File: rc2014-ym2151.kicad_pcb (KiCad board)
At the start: 2 copper layers, 100 x 50 mm, 36 parts, among them CON1 SJ1-3523N, J1 Conn_01x03, P1 RC2014 BUS, U1 74HCT688, U2 YM2151, U3 YM3012, U4 NJM4556, U5 NJM4556, X1 3.579545MHz

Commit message: add bits lurking around
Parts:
- C10, C11: footprint Capacitor_THT:CP_Radial_D7.5mm_P2.50mm -> Capacitor_THT:CP_Radial_D5.0mm_P2.50mm
- C7: footprint Capacitor_THT:C_Disc_D3.8mm_W2.6mm_P2.50mm -> Capacitor_THT:C_Radial_D4.0mm_H7.0mm_P1.50mm
- J1: footprint Connector_PinHeader_2.54mm:PinHeader_1x07_P2.54mm_Vertical -> Connector_PinHeader_2.54mm:PinHeader_1x06_P2.54mm_Vertical
- moved C7 1.56 mm to (104.0, 117.8)
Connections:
- J1 pad 3: /~IRQ -> GND
- J1 pad 4: GND -> VSS
- J1 pad 5: VSS -> VDD
- J1 pad 6: VDD -> VCC
- P1 pad 22: (no net) -> /~INT
- U2 pad 2: /~IRQ -> /~INT
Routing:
- net /~IRQ: track 41.7 -> 0.00 mm, vias 1 -> 0
- net /~INT: track 0.00 -> 11.0 mm, vias 0 -> 1
- net VSS: track 78.3 -> 75.8 mm
- net VCC: track 165.6 -> 163.1 mm
- net VDD: track 109.3 -> 106.8 mm
- net /RB: track 18.8 -> 20.5 mm
- net Net-(R1-Pad1): track 19.1 -> 20.1 mm
- net /~IORQ: track 50.8 -> 51.8 mm
- net /~CS: track 59.9 -> 60.5 mm
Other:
- board text added: "JLCJLCJLCJLC"
- board text removed: "~IRQ"

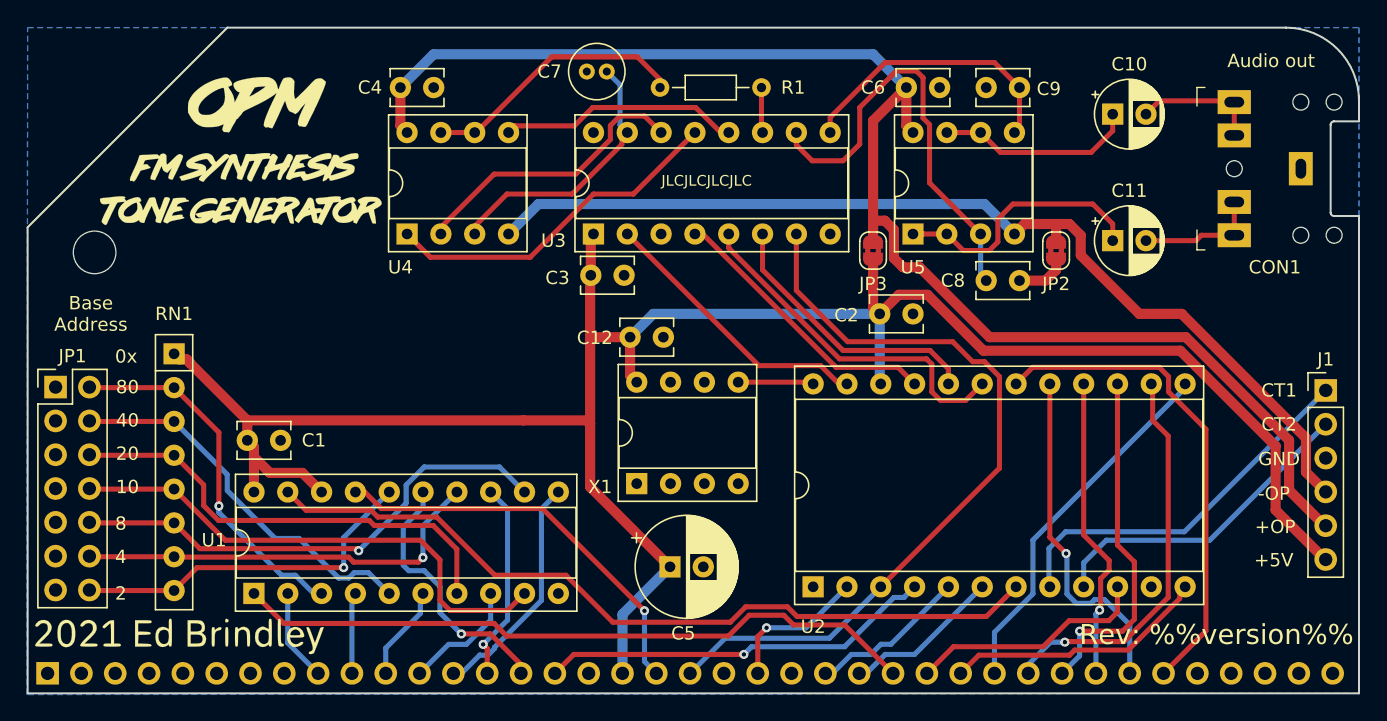
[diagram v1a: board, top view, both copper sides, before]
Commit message: Update to Kicad 6
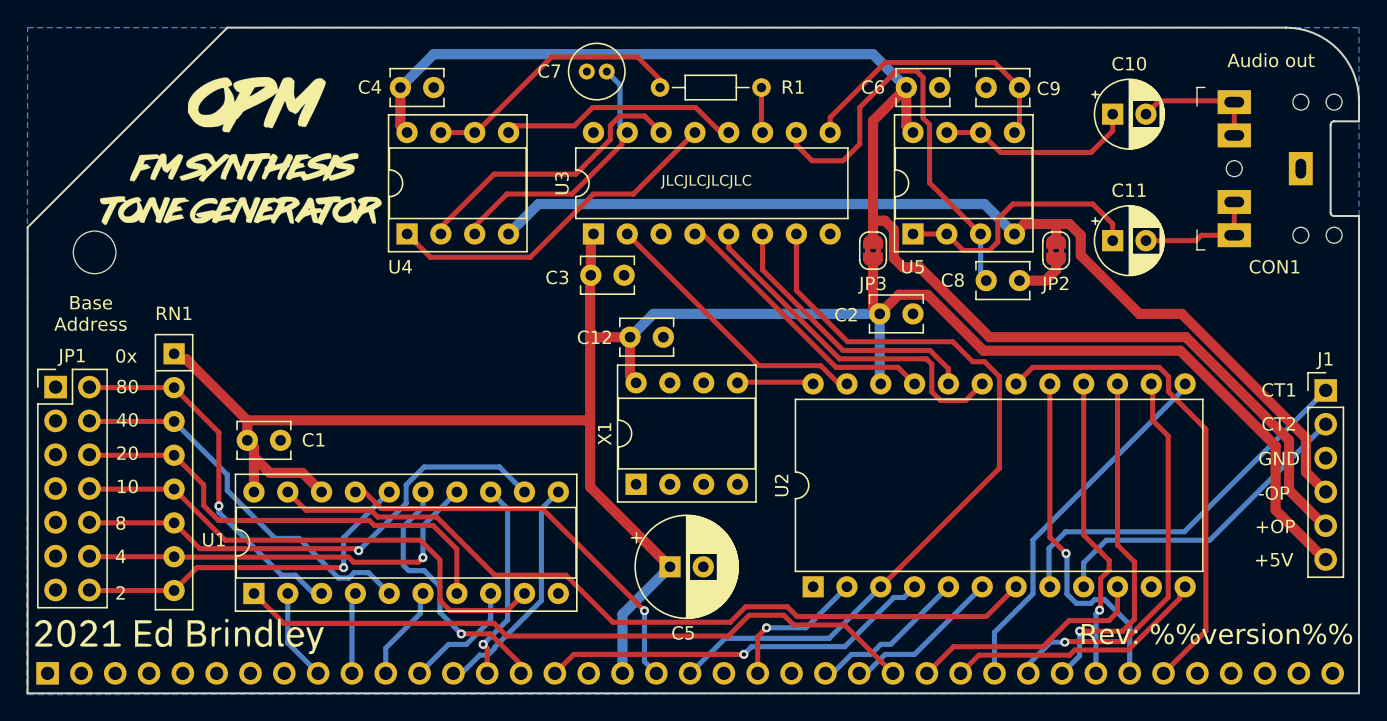
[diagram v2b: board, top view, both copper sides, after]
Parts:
- U2: footprint Package_DIP:DIP-24_W15.24mm_Socket -> Package_DIP:DIP-24_W15.24mm
- U3: footprint Package_DIP:DIP-16_W7.62mm_Socket -> Package_DIP:DIP-16_W7.62mm
- moved X1 0.07 mm to (106.2, 148.8)
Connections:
- net /~CS renamed /~{CS}
- net /~INT renamed /~{INT}
- net /~IORQ renamed /~{IORQ}
- net /~RD renamed /~{RD}
- net /~RESET renamed /~{RESET}
- net /~WR renamed /~{WR}
- P1 pad 1: (no net) -> unconnected-(P1-Pad1)
- P1 pad 2: (no net) -> unconnected-(P1-Pad2)
- P1 pad 21: (no net) -> unconnected-(P1-Pad21)
- P1 pad 23: (no net) -> unconnected-(P1-Pad23)
- P1 pad 3: (no net) -> unconnected-(P1-Pad3)
- P1 pad 35: (no net) -> unconnected-(P1-Pad35)
- P1 pad 36: (no net) -> unconnected-(P1-Pad36)
- P1 pad 37: (no net) -> unconnected-(P1-Pad37)
- P1 pad 38: (no net) -> unconnected-(P1-Pad38)
- P1 pad 39: (no net) -> unconnected-(P1-Pad39)
- P1 pad 4: (no net) -> unconnected-(P1-Pad4)
- P1 pad 5: (no net) -> unconnected-(P1-Pad5)
- P1 pad 6: (no net) -> unconnected-(P1-Pad6)
- P1 pad 7: (no net) -> unconnected-(P1-Pad7)
- P1 pad 8: (no net) -> unconnected-(P1-Pad8)
- X1 pad 1: (no net) -> unconnected-(X1-Pad1)
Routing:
- net /RB: track 20.5 -> 19.3 mm
- net VCC: track 163.1 -> 162.0 mm
- net /A1: track 19.9 -> 19.2 mm
- net Net-(JP1-Pad2): track 27.4 -> 26.7 mm
- net /A3: track 17.6 -> 17.0 mm
- net /R: track 19.8 -> 19.2 mm
- net /DAC_CLK: track 21.2 -> 20.6 mm
- net /TO_BUFF: track 18.1 -> 17.5 mm
- net /VOUT_CH1: track 32.8 -> 32.2 mm
- net /DAC_DATA: track 21.2 -> 20.6 mm
- net /D1: track 19.8 -> 19.3 mm
- net /VOUT_CH2: track 21.4 -> 20.8 mm
- net /~{WR}: track 11.9 -> 11.4 mm
- net /~{RD}: track 11.9 -> 11.4 mm
- net /BC: track 21.6 -> 21.1 mm
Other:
- net class Default removed
- net class IO removed
- net class analogue removed
- net class gnd removed
- net class vcc removed

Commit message: Tidy up schematic further
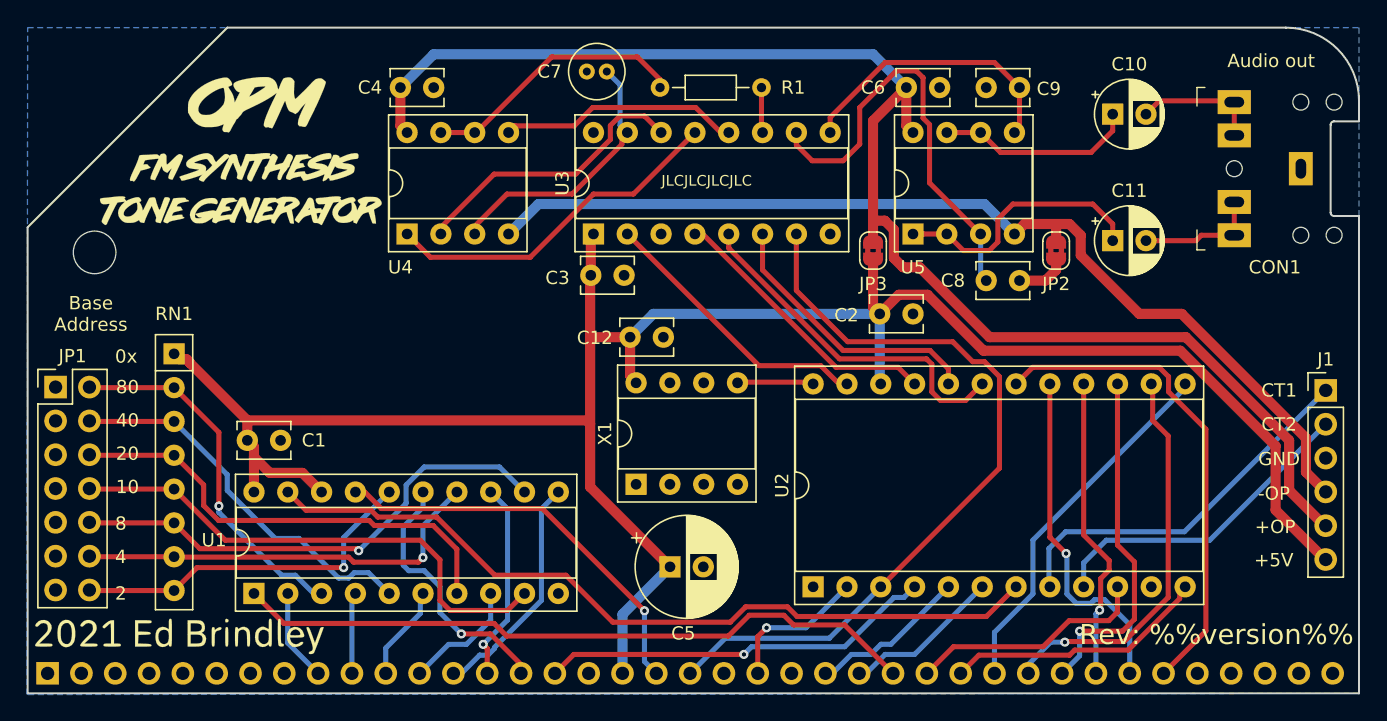
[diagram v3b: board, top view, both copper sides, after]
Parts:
- U2: footprint Package_DIP:DIP-24_W15.24mm -> Package_DIP:DIP-24_W15.24mm_Socket
- U3: footprint Package_DIP:DIP-16_W7.62mm -> Package_DIP:DIP-16_W7.62mm_Socket

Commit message: remove silk that clashes, another date fix
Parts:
- removed the G*** at (134.3, 148.8)

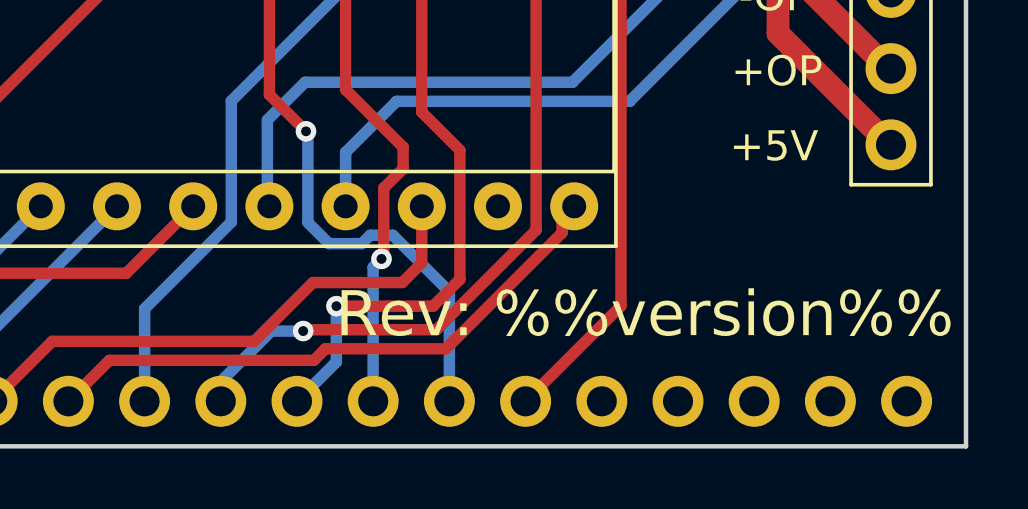
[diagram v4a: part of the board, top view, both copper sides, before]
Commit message: date replacement
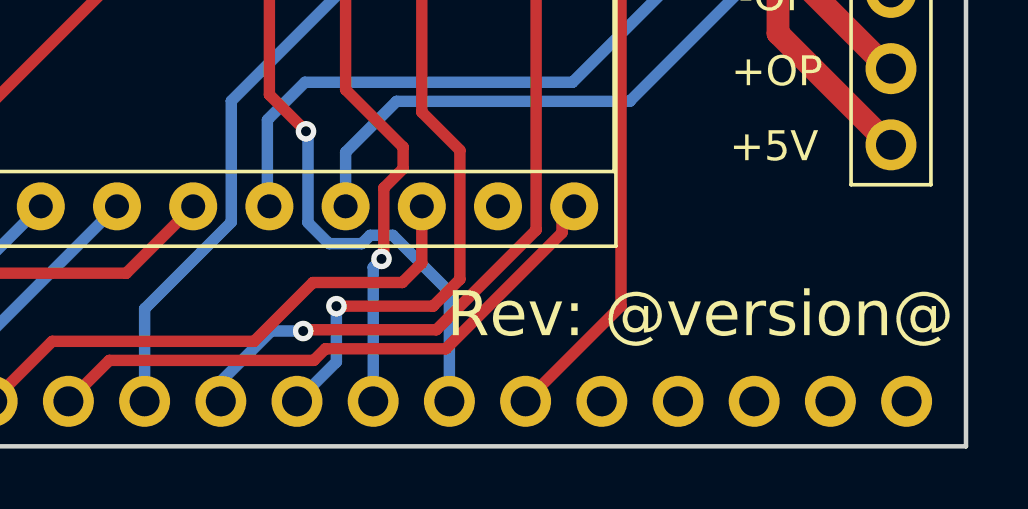
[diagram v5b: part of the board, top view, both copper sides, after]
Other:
- board text added: "Rev: @version@"
- board text removed: "Rev: %%version%%"
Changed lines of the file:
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@@
   (title_block
     (title "RC2014 YM2151 sound card")
-    (date "%%date%%")
-    (rev "%%version%%")
+    (date "@date@")
+    (rev "@version@")
   )
   (layers
@@
     (effects (font (size 1 1) (thickness 0.15)))
   )
-  (gr_text "Rev: %%version%%" (at 160.1 160.1) (layer "F.SilkS")
+  (gr_text "Rev: @version@" (at 160.1 160.1) (layer "F.SilkS")
     (effects (font (size 1.5 1.5) (thickness 0.3)) (justify right))
   )

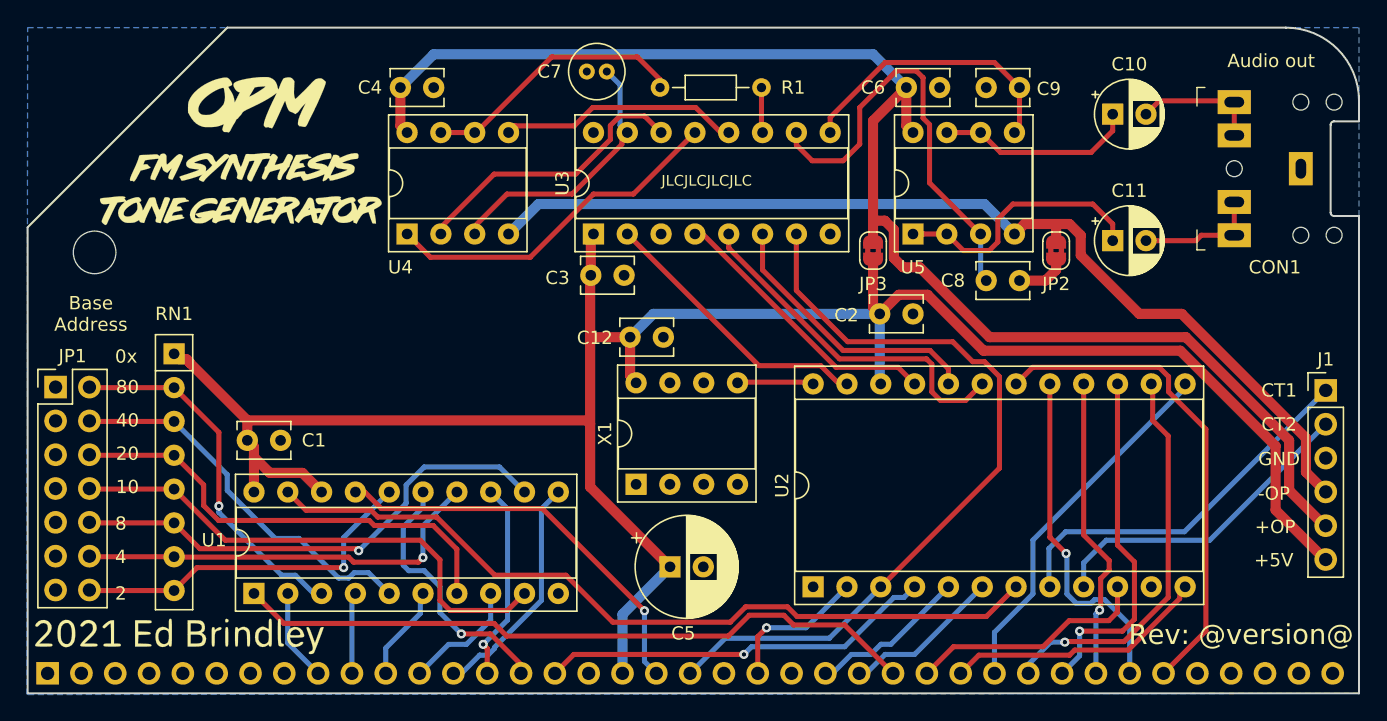
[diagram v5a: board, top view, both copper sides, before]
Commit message: Use Aisler DRC
Update README.md

change board outline

wip
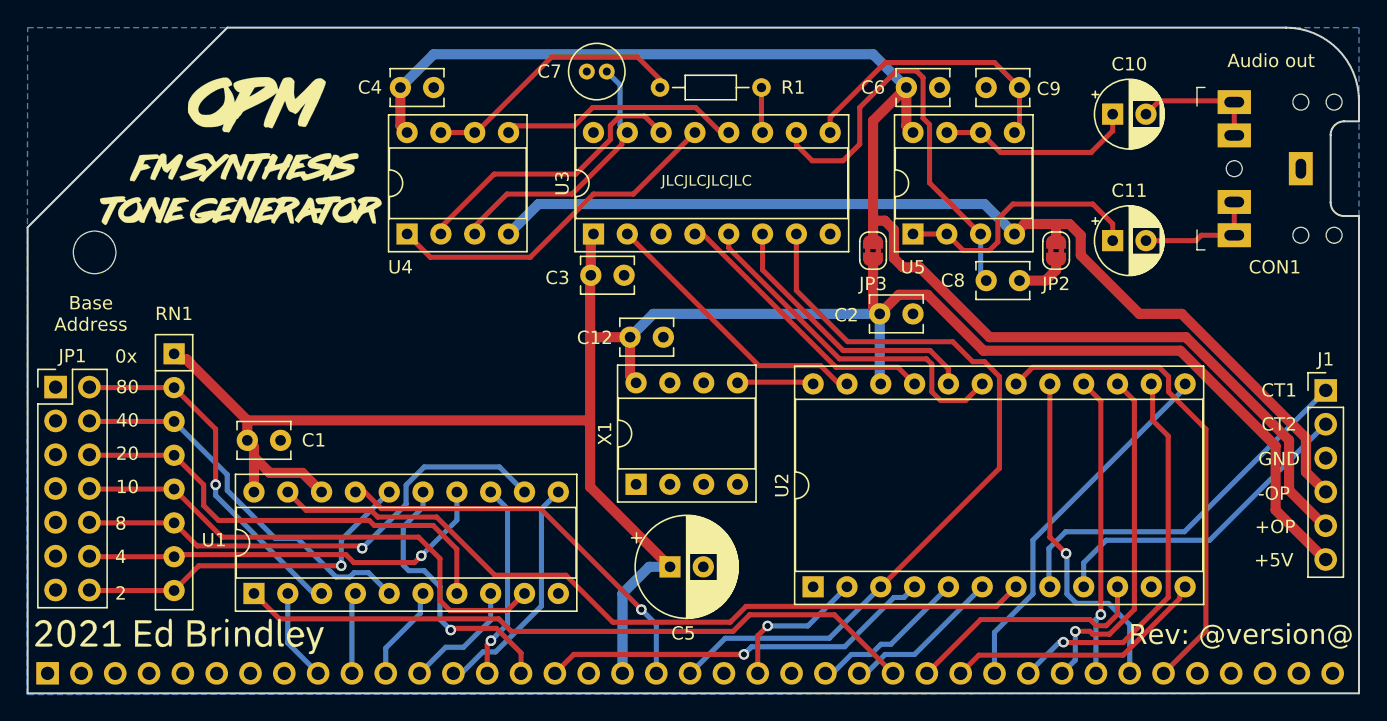
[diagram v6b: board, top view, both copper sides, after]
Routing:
- net VCC: track 162.0 -> 162.9 mm
- net /A1: track 19.2 -> 20.1 mm
- net /R: track 19.2 -> 19.8 mm
- net /~{CS}: track 60.5 -> 59.9 mm
- net Net-(JP1-Pad2): track 26.7 -> 26.1 mm
- net /D5: track 22.9 -> 22.4 mm
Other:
- outline, holes or cut-outs redrawn
- rule pad_to_mask_clearance: 0.2 -> 0

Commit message: remove dubious silkscreen
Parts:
- removed the G*** at (71.9, 160.2)
- removed the G*** at (115.2, 125.9)
- removed the G*** at (148.4, 117.5)
- added G***: LOGO, LOGO, B.Cu at (132.2, 149.1)
- moved G3 4.75 mm to (78.0, 124.5)
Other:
- outline, holes or cut-outs redrawn
- board text added: "2021-2022 Ed Brindley"
- board text added: "No jumper = enabled Base address with no jumpers is 0xFF"

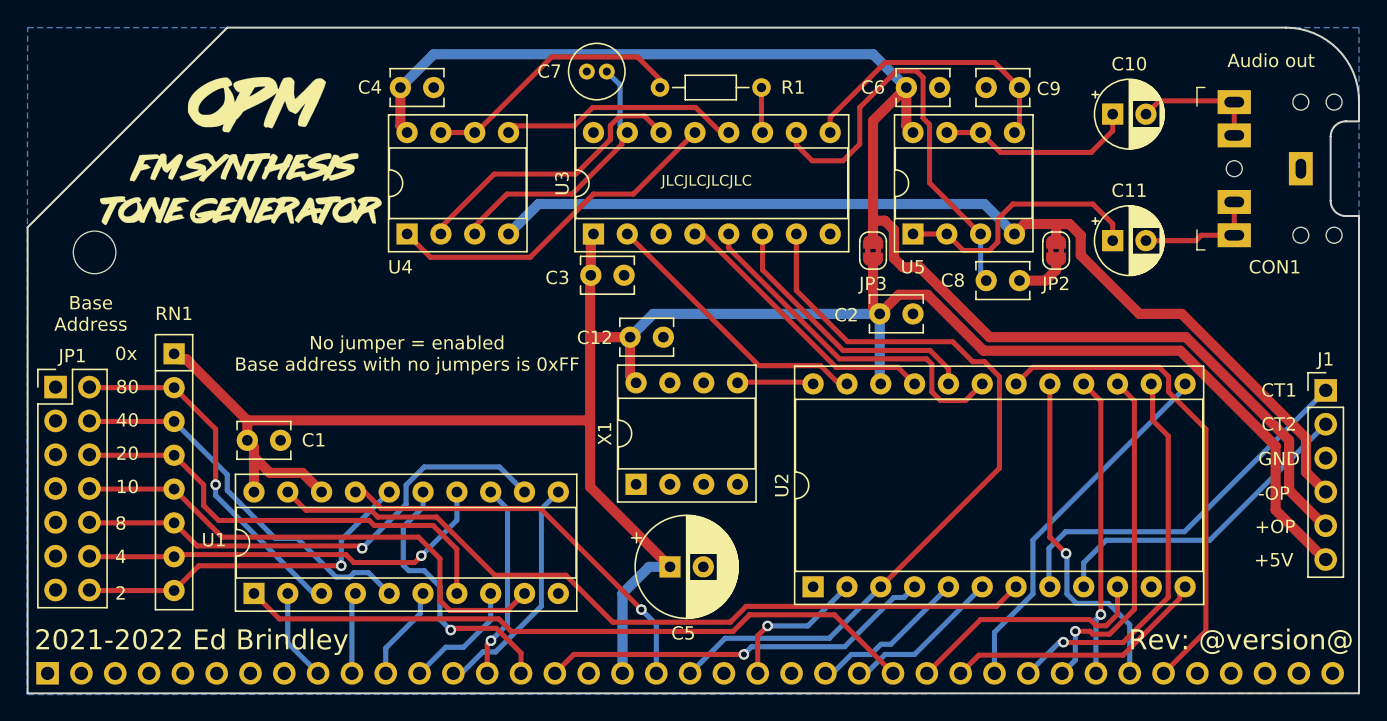
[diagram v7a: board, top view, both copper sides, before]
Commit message: migrate to kicad 9 - fix most of the ERC and DRC issues, use current library symbols/footprints
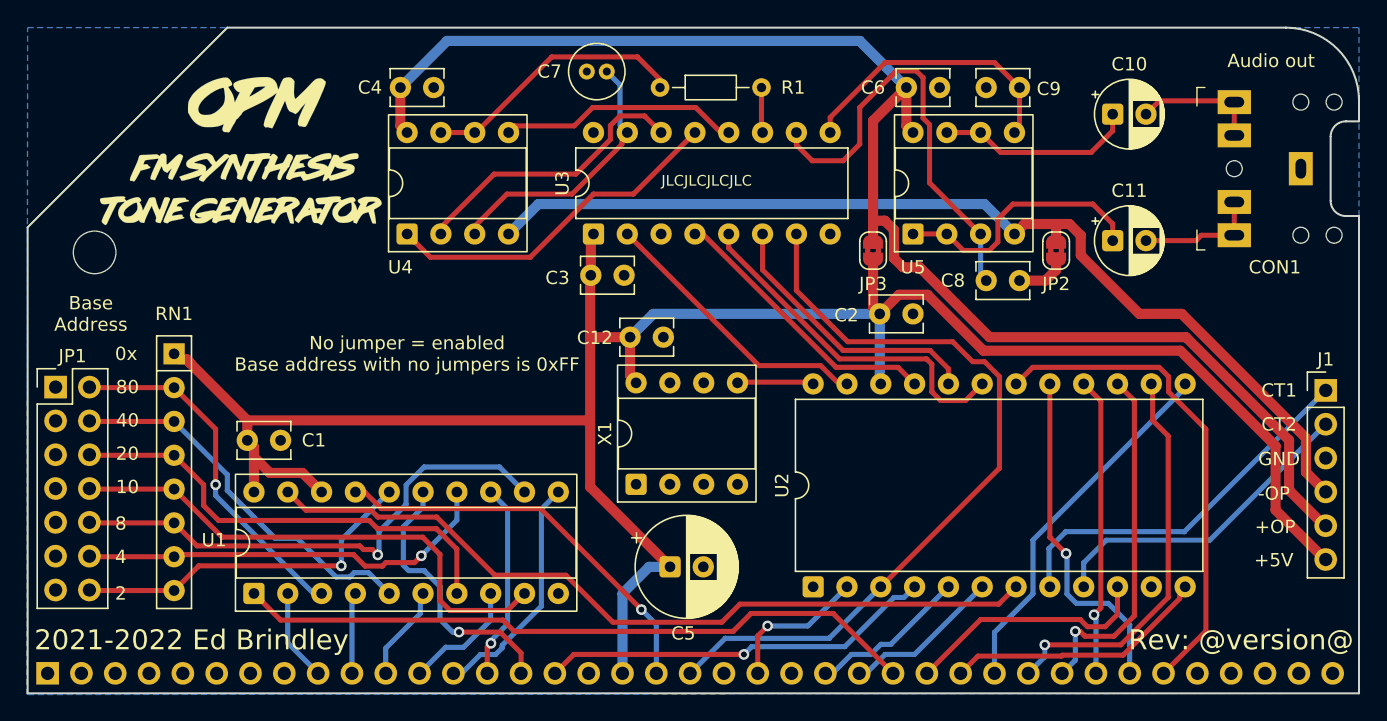
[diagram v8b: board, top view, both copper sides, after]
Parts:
- G1: footprint electrified:opm -> local:opm
- J1: value Conn_01x03 -> Debug connector
- U2: footprint Package_DIP:DIP-24_W15.24mm_Socket -> Package_DIP:DIP-24_W15.24mm
- U3: footprint Package_DIP:DIP-16_W7.62mm_Socket -> Package_DIP:DIP-16_W7.62mm
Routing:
- net Net-(JP1-Pin_10): track 37.6 -> 39.0 mm
- net VDD: track 106.7 -> 107.6 mm
- net /D3: track 29.3 -> 29.8 mm
